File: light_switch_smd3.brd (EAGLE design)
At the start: 35.4 x 35.1 mm, 19 parts

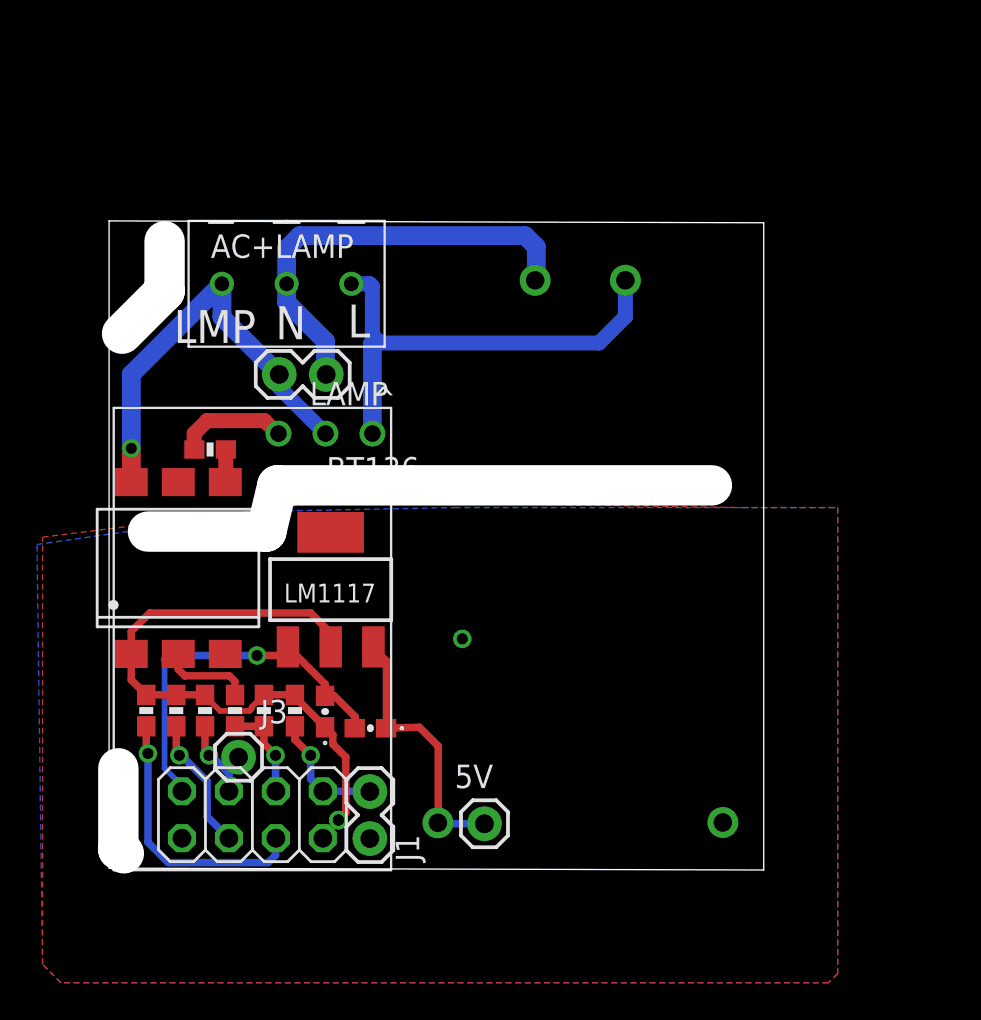
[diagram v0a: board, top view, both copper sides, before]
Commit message: major update. added second relay circuit, redesigned board
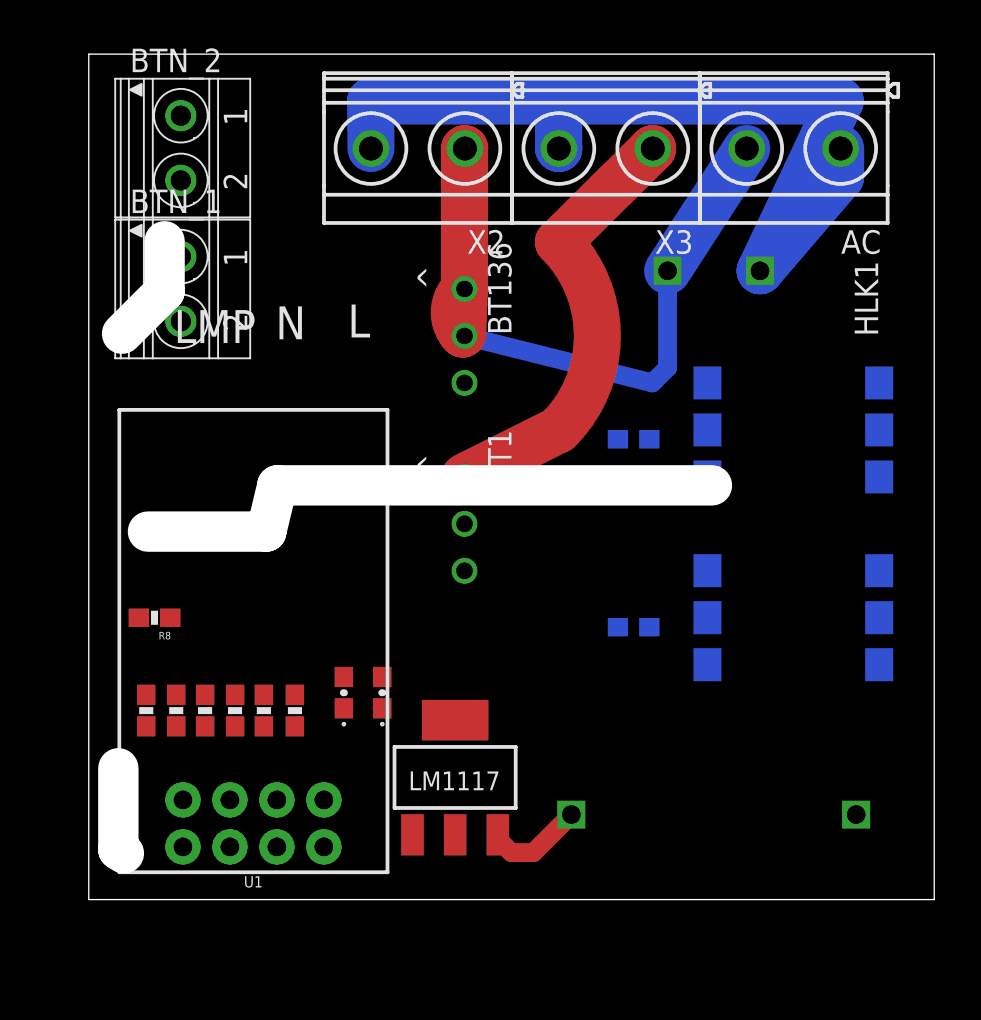
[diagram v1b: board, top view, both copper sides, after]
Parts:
- removed 5V, J3: (no value), SparkFun-Connectors:1X01
- removed AC+LAMP: DG350-3.5-03P, myblog_library:DG350-3.5-03P
- removed J1, LAMP: (no value), SparkFun-Connectors:1X02
- removed U$1: HI-LINK5V-ACDC, myblog_library:AC5V
- removed U$2: ESP8266-01, myblog_library:ESP8266-01
- added AC, X2, X3: MKDSN1,5/2-5,08, con-phoenix-508:MKDSN1,5/2-5,08
- added BT1: BT136, myblog_library:BT136-PKG
- added BTN_1, BTN_2: 1751248, con-phoenix-350:1751248
- added HLK1: HLK-PM013W, HLK-PM01:HLK-PM01
- added OK2: MOC3033S, optocoupler:DIL6-SMD
- added R10: 470, SparkFun-Resistors:0603-RES
- added R8: 3.3K, SparkFun-Resistors:0603-RES
- added R9: 430, SparkFun-Resistors:0603-RES
- added U1: ESP8266_ESP-01, SparkFun-RF:ESP8266_ESP-01
- moved OK1 34.1 mm to (38.1, 25.4), flipped to the bottom, turned to 270 degrees
- moved R7 22.9 mm to (29.5, 24.9), flipped to the bottom, turned to 0 degrees
- moved LM1117 12.2 mm to (19.8, 6.60)
- moved BT136 9.19 mm to (20.3, 30.5), turned to 270 degrees
- moved C2 2.02 mm to (15.9, 11.2), turned to 270 degrees
- moved C1 1.44 mm to (13.8, 11.2)
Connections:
- removed net N$11: AC+LAMP.P$2, LAMP.2, U$1.AC2
- removed net N$12: AC+LAMP.P$3, BT136.T1, U$1.AC1
- new net +3V3: C1.A, LM1117.2, OK1.1, OK2.1, R2.2, R3.1, R8.2, U1.4
- new net +5V: C2.A, HLK1.P$4, LM1117.3
- new net GPIO0: BTN_1.1, R5.1, U1.6
- new net GPIO2: R6.1, R8.1, U1.7
- new net N$27: R4.1
- new net N$28: R5.2
- new net N$4: BT136.T1, X2.1
- new net RXD: BTN_2.1, R2.1, U1.5
- new net TXD: R9.1
- new net VPP: AC.2, BT1.T2, BT136.T2, HLK1.P$2, OK1.6, OK2.6
- new net VSS: AC.1, HLK1.P$1, X2.2, X3.2
- net GND: now also BTN_1.2, BTN_2.2, HLK1.P$3, U1.8; no longer J1.1, U$1.5V_GND, U$2.8
- net N$1: now also U1.3; no longer J1.2, U$2.2
- net N$13: now also R1.1; no longer 5V.1, C2.A, LM1117.3, U$1.5V_VCC
- net N$14: now also BT1.G, R10.2; no longer J3.1, R5.1, U$2.6
- net N$2: now also OK2.2, R9.2; no longer R2.1, U$2.5
- net N$26: now also U1.2; no longer U$2.3
- net N$3: now also OK2.4, R10.1; no longer C1.A, LM1117.2, OK1.1, R1.1, R2.2, R3.1, R4.1, R5.2, U$2.1
- net N$8: now also BT1.T1, X3.1; no longer AC+LAMP.P$1, BT136.T2, LAMP.1, OK1.6
- net N$9: now also U1.1; no longer R6.1, U$2.4
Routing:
- net VSS: track 0.00 -> 51.5 mm
- net N$3: track 34.4 -> 0.00 mm, vias 1 -> 0
- net N$12: track 25.4 -> 0.00 mm
- net VPP: track 0.00 -> 24.8 mm
- net N$11: track 23.6 -> 0.00 mm
- net GND: track 20.7 -> 0.00 mm, vias 2 -> 0
- net N$26: track 14.8 -> 0.00 mm, vias 1 -> 0
- net N$13: track 14.7 -> 0.00 mm
- net N$4: track 0.00 -> 12.5 mm
- net N$2: track 7.29 -> 0.00 mm, vias 1 -> 0
- net N$1: track 6.68 -> 0.00 mm, vias 1 -> 0
- net N$14: track 6.48 -> 0.00 mm, vias 1 -> 0
- net N$6: track 6.00 -> 0.00 mm
- net +5V: track 0.00 -> 5.36 mm
- net N$9: track 5.34 -> 0.00 mm, vias 1 -> 0
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- removed copper zone on layer 1, net GND
- removed copper zone on layer 16, net GND
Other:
- board size 35.4 x 35.1 mm -> 45.7 x 45.7 mm

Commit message: almost ready for production. some descriptions needs adjusting.
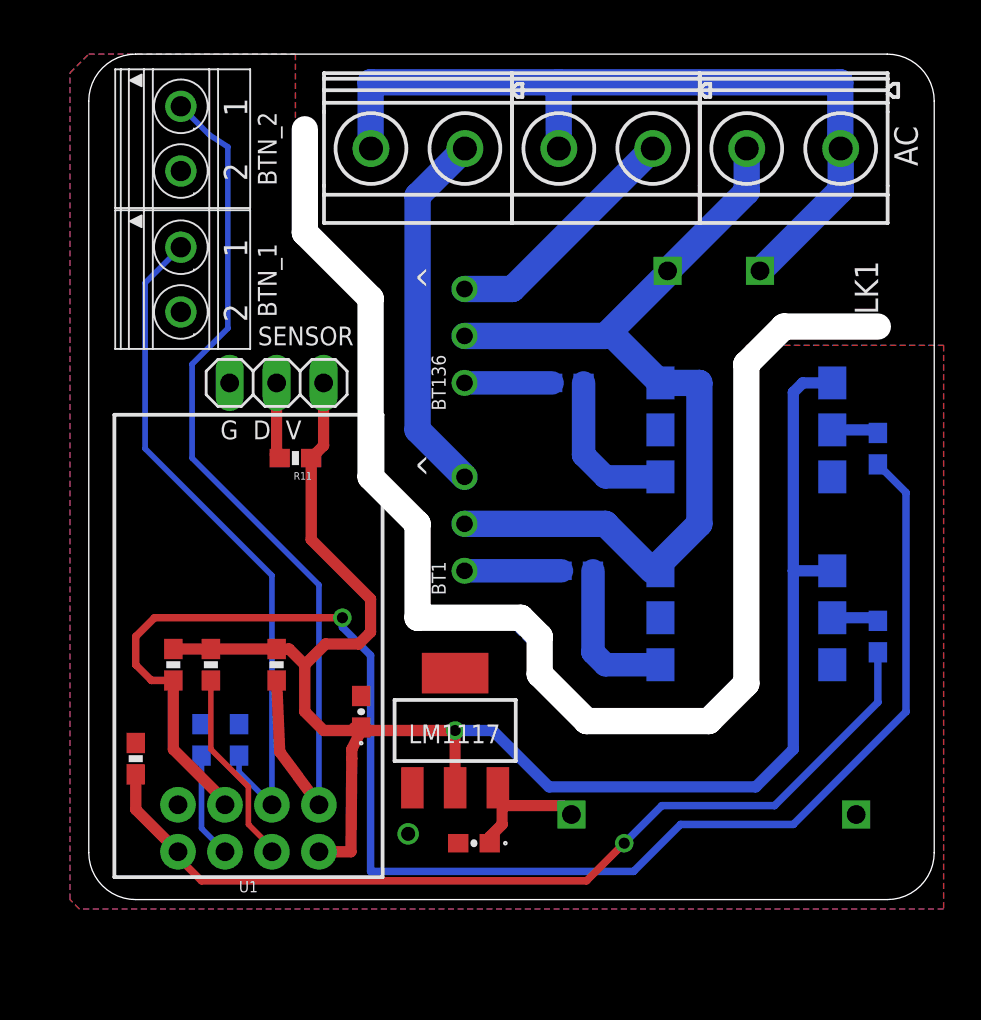
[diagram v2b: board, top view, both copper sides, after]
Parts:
- added R11: 3.3K, SparkFun-Resistors:0603-RES
- added SENSOR: (no value), pinhead:1X03
- moved R6 37.5 mm to (42.7, 24.4), flipped to the bottom
- moved R9 31.2 mm to (42.7, 14.2), flipped to the bottom, turned to 90 degrees
- moved C2 9.53 mm to (20.8, 3.05), turned to 0 degrees
- moved R4 7.40 mm to (2.54, 7.62)
- moved R2 5.97 mm to (10.2, 12.7)
- moved R3 5.18 mm to (6.60, 12.7)
- moved R7 4.68 mm to (25.9, 27.9)
- moved R10 4.31 mm to (26.4, 17.8)
- moved R1 3.38 mm to (6.10, 8.64), flipped to the bottom
- moved R8 2.74 mm to (4.57, 12.7), turned to 90 degrees
- moved LM1117 2.54 mm to (19.8, 9.14)
- moved OK1 2.54 mm to (35.6, 25.4)
- moved OK2 2.54 mm to (35.6, 15.2)
- moved R5 2.43 mm to (8.13, 8.64), flipped to the bottom
- moved C1 1.39 mm to (14.7, 10.2)
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- renumbered X2 to OUT_2, X3 to OUT_1
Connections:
- net N$1 renamed RST
- net N$26 renamed CH_PD
- removed net N$9: R4.2, U1.1
- new net DATA: R11.2, SENSOR.2
- net +3V3: now also R11.1, SENSOR.3
- net GND: now also SENSOR.1
- net N$4: now also OUT_1.1; no longer OUT_2.1
- net N$8: now also OUT_2.1; no longer OUT_1.1
- net TXD: now also R4.2, U1.1
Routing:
- net +3V3: track 0.00 -> 93.8 mm, vias 0 -> 1
- net GPIO2: track 0.00 -> 84.3 mm, vias 0 -> 1
- net TXD: track 0.00 -> 50.5 mm, vias 0 -> 1
- net RXD: track 0.00 -> 50.0 mm
- net GPIO0: track 0.00 -> 37.2 mm
- net VPP: track 24.8 -> 49.7 mm
- net RST: track 0.00 -> 10.6 mm
- net N$7: track 0.00 -> 8.54 mm
- net N$3: track 0.00 -> 8.33 mm
- net VSS: track 51.5 -> 44.6 mm
- net CH_PD: track 0.00 -> 5.73 mm
- net N$14: track 0.00 -> 5.25 mm
- net N$6: track 0.00 -> 4.74 mm
- net DATA: track 0.00 -> 4.13 mm
- net N$8: track 23.0 -> 19.9 mm
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- added copper zone on layer 1, net GND
- added copper zone on layer 16, net GND
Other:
- outline, holes or cut-outs redrawn
- board text added: "Double channel WiFi switch 2019 m4system.pl"
- board text added: "G D V"
- board text removed: "Hristo Borisov Light Switch Prototype Rev. 0.8"
- board text removed: "LMP"

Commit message: minor bugs fixed
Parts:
- R11: value 3.3K -> 4.7K
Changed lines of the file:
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@@
 <grid distance="0.1" unitdist="inch" unit="inch" style="dots" multiple="1" display="yes" altdistance="0.02" altunitdist="inch" altunit="inch"/>
 <layers>
-<layer number="1" name="Top" color="4" fill="1" visible="yes" active="yes"/>
+<layer number="1" name="Top" color="4" fill="1" visible="no" active="yes"/>
 <layer number="2" name="Route2" color="1" fill="3" visible="yes" active="yes"/>
 <layer number="3" name="Route3" color="4" fill="3" visible="no" active="no"/>
@@
 <layer number="14" name="Route14" color="1" fill="6" visible="no" active="no"/>
 <layer number="15" name="Route15" color="4" fill="6" visible="yes" active="yes"/>
-<layer number="16" name="Bottom" color="1" fill="1" visible="yes" active="yes"/>
+<layer number="16" name="Bottom" color="1" fill="1" visible="no" active="yes"/>
 <layer number="17" name="Pads" color="2" fill="1" visible="yes" active="yes"/>
 <layer number="18" name="Vias" color="2" fill="1" visible="yes" active="yes"/>
@@
 <wire x1="11.684" y1="36.068" x2="11.684" y2="41.656" width="1.4224" layer="46"/>
 <text x="34.828" y="44.784" size="1.778" layer="26" rot="MR180">L</text>
-<text x="40.7" y="43" size="1.778" layer="26" rot="MR0">N</text>
-<text x="2.54" y="17.78" size="0.8128" layer="26" rot="MR90">Double channel
+<text x="41.716" y="43" size="1.778" layer="26" rot="MR0">N</text>
+<text x="2.54" y="12.7" size="0.8128" layer="26" font="vector" ratio="10" rot="MR90">Double channel
 WiFi switch
 2019 m4system.pl</text>
@@
 <element name="R5" library="SparkFun-Resistors" package="0603-RES" value="3.3K" x="8.128" y="8.636" smashed="yes" rot="MR90">
 <attribute name="PROD_ID" value="RES-11057" x="8.128" y="8.636" size="1.778" layer="28" rot="MR90" display="off"/>
-<attribute name="VALUE" x="9.144" y="7.112" size="0.4064" layer="27" font="vector" rot="MR90"/>
+<attribute name="VALUE" x="9.144" y="7.112" size="0.4064" layer="28" font="vector" rot="MR90"/>
 </element>
 <element name="R6" library="SparkFun-Resistors" package="0603-RES" value="430" x="42.672" y="24.384" smashed="yes" rot="MR90">
@@
 </element>
 <element name="R7" library="SparkFun-Resistors" package="0603-RES" value="470" x="25.908" y="27.94" smashed="yes" rot="MR0">
-<attribute name="VALUE" x="27.005" y="26.616" size="0.8128" layer="28" font="vector" rot="MR0"/>
+<attribute name="VALUE" x="26.924" y="26.416" size="0.4064" layer="28" font="vector" rot="MR0"/>
 </element>
 <element name="LM1117" library="SparkFun-PowerIC" package="SOT223" value="LM1117" x="19.812" y="9.144" smashed="yes">
-<attribute name="NAME" x="17.2865" y="8.4525" size="1.016" layer="25"/>
+<attribute name="NAME" x="17.2865" y="8.4525" size="0.6096" layer="25" font="vector"/>
 <attribute name="PROD_ID" value="VREG-08170" x="19.812" y="9.144" size="1.778" layer="27" display="off"/>
 </element>
@@
 <attribute name="MF" value="" x="5.08" y="33.528" size="1.778" layer="27" rot="R270" display="off"/>
 <attribute name="MPN" value="" x="5.08" y="33.528" size="1.778" layer="27" rot="R270" display="off"/>
-<attribute name="NAME" x="10.16" y="31.496" size="1.016" layer="25" font="vector" rot="R90"/>
+<attribute name="NAME" x="10.16" y="32.512" size="1.016" layer="25" font="vector" rot="R90"/>
 <attribute name="OC_FARNELL" value="unknown" x="5.08" y="33.528" size="1.778" layer="27" rot="R270" display="off"/>
 <attribute name="OC_NEWARK" value="unknown" x="5.08" y="33.528" size="1.778" layer="27" rot="R270" display="off"/>
@@
 <attribute name="MF" value="" x="5.08" y="41.148" size="1.778" layer="27" rot="R270" display="off"/>
 <attribute name="MPN" value="" x="5.08" y="41.148" size="1.778" layer="27" rot="R270" display="off"/>
-<attribute name="NAME" x="10.16" y="38.608" size="1.016" layer="25" font="vector" rot="R90"/>
+<attribute name="NAME" x="10.16" y="40.132" size="1.016" layer="25" font="vector" rot="R90"/>
 <attribute name="OC_FARNELL" value="unknown" x="5.08" y="41.148" size="1.778" layer="27" rot="R270" display="off"/>
 <attribute name="OC_NEWARK" value="unknown" x="5.08" y="41.148" size="1.778" layer="27" rot="R270" display="off"/>
@@
 </element>
 <element name="SENSOR" library="pinhead" package="1X03" value="" x="10.16" y="27.94" smashed="yes">
-<attribute name="NAME" x="9.144" y="29.972" size="1.016" layer="25" font="vector"/>
+<attribute name="NAME" x="9.144" y="29.972" size="0.8128" layer="25" font="vector"/>
 <attribute name="VALUE" x="6.35" y="24.765" size="1.27" layer="27"/>
 </element>
-<element name="R11" library="SparkFun-Resistors" package="0603-RES" value="3.3K" x="11.176" y="23.876" smashed="yes" rot="R180">
+<element name="R11" library="SparkFun-Resistors" package="0603-RES" value="4.7K" x="11.176" y="23.876" smashed="yes" rot="R180">
 <attribute name="NAME" x="12.065" y="23.114" size="0.4064" layer="25" font="vector" rot="R180"/>
 <attribute name="PROD_ID" value="RES-11057" x="11.176" y="23.876" size="1.778" layer="27" rot="R180" display="off"/>

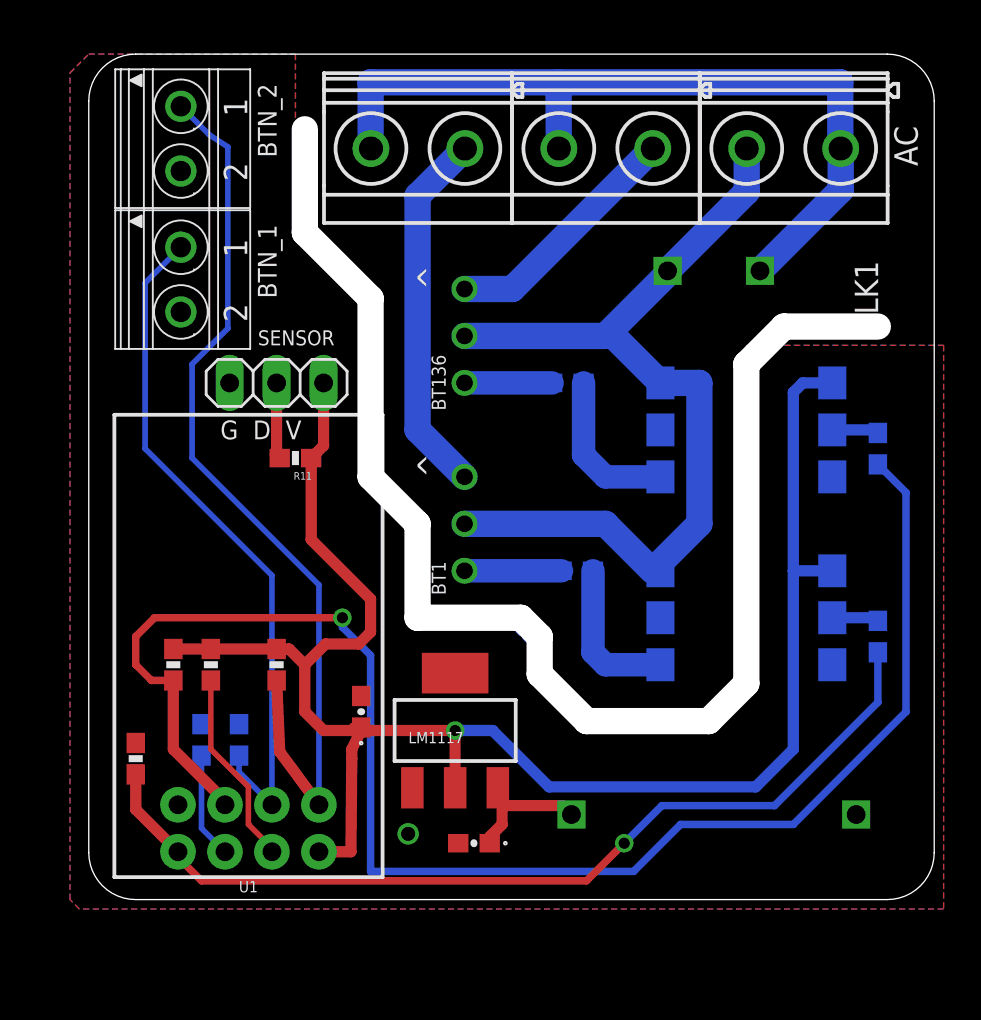
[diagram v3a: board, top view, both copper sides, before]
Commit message: sligthly bigger smd parts, for easier soldering
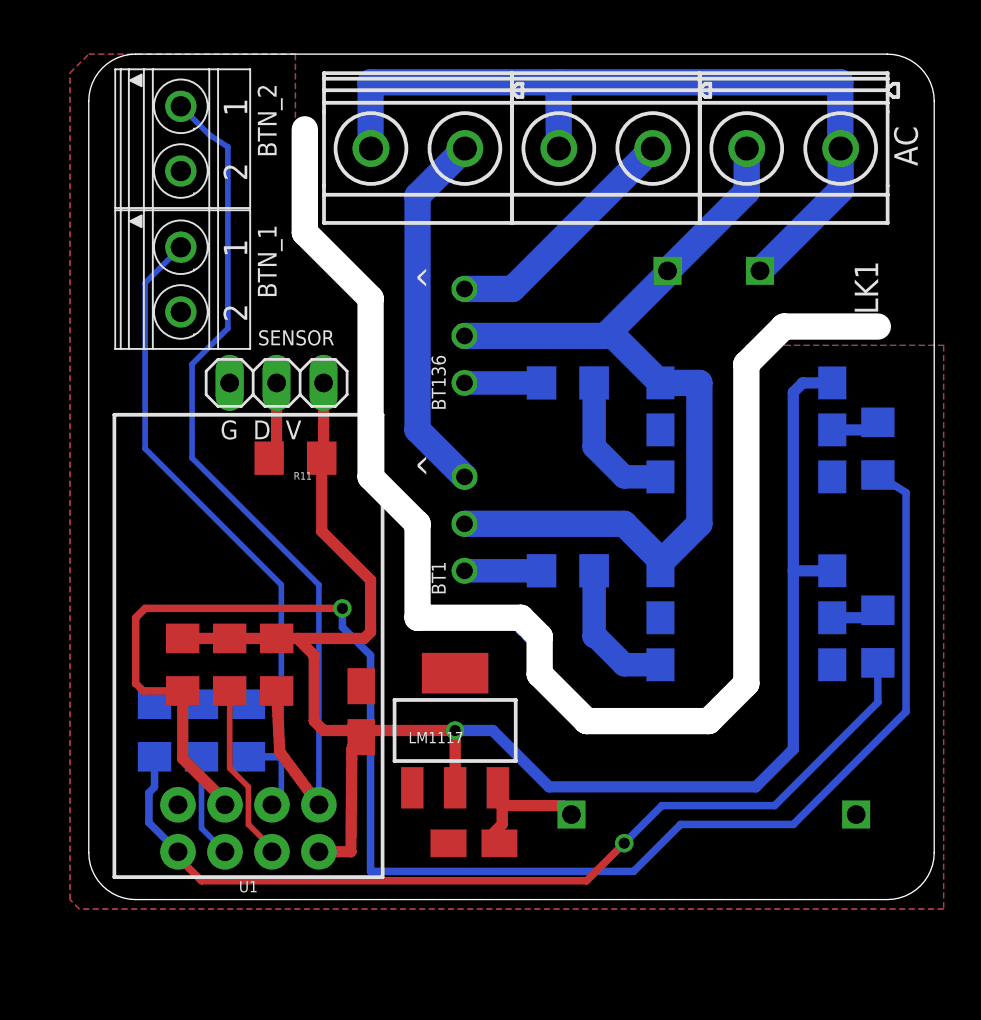
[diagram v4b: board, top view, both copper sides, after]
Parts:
- C1, C2: device SparkFun-Capacitors:0603-POL -> resistor:A/3216-18R
- R1, R10, R11, R2, R3, R4, R5, R6, R7, R8, R9: device SparkFun-Resistors:0603-RES -> resistor:R1206
- moved R4 1.83 mm to (3.56, 9.14), flipped to the bottom
- moved R3 1.02 mm to (7.62, 12.7)
- moved R5 0.72 mm to (8.64, 9.14)
- moved R1 0.51 mm to (6.10, 9.14)
- moved R8 0.51 mm to (5.08, 12.7)
- moved R10 0.51 mm to (25.9, 17.8)
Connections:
- net +3V3: now also C1.+; no longer C1.A
- net +5V: now also C2.+; no longer C2.A
- net GND: now also C1.-, C2.-; no longer C1.K, C2.K
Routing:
- net GPIO2: track 84.3 -> 85.8 mm
- net GPIO0: track 37.2 -> 36.0 mm
- net N$14: track 5.25 -> 4.17 mm
- net RST: track 10.6 -> 9.64 mm
- net N$7: track 8.54 -> 7.71 mm
- net N$6: track 4.74 -> 4.17 mm
- net RXD: track 50.0 -> 49.4 mm
- net N$3: track 8.33 -> 7.76 mm
- net +3V3: track 93.8 -> 94.3 mm

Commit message: kosmetyczne poprawki, wersja wysłana do produkcji
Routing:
- net VSS: track 44.6 -> 41.5 mm
- net VPP: track 50.1 -> 51.1 mm
